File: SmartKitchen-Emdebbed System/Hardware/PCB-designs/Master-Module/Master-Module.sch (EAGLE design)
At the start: 20 parts, among them IC2 7805DT, J1 RJ11-2L-B, J2 RJ11-2L-B, J3 RJ11-2L-B, J4 RJ11-2L-B, Q1 BSS123, X1 K375M

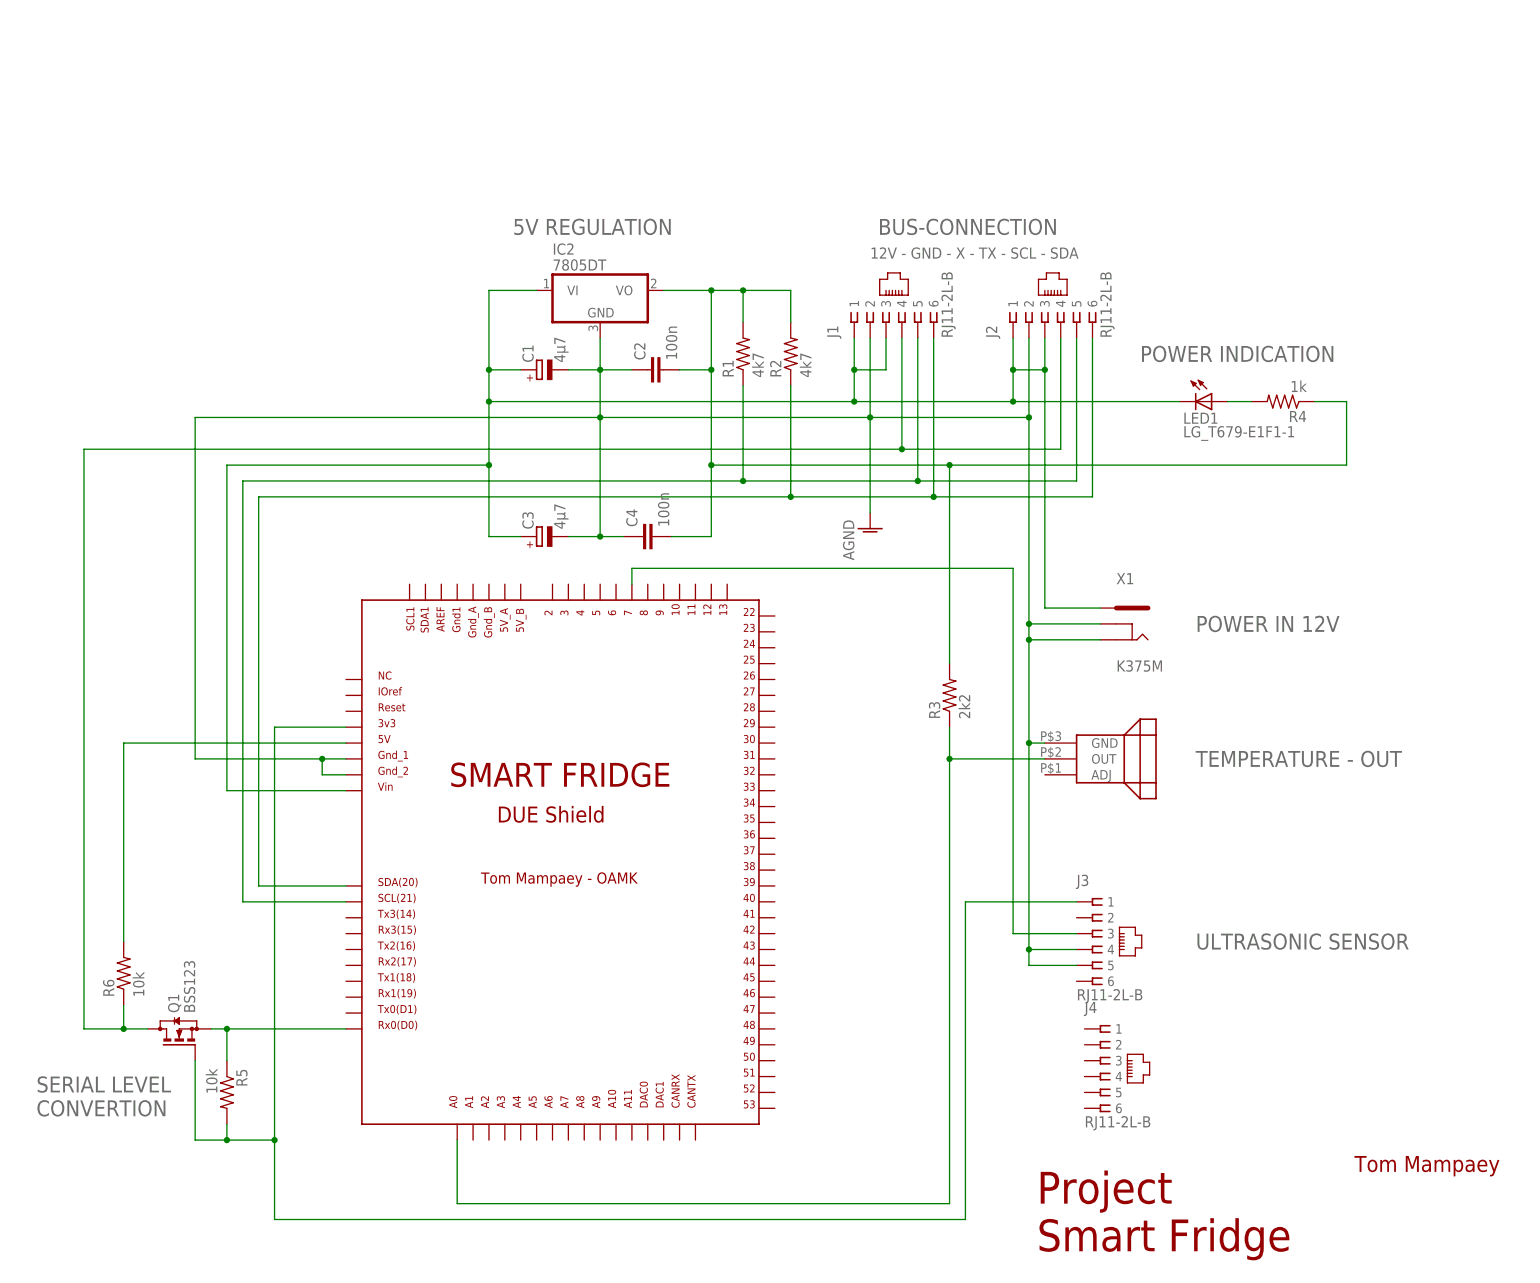
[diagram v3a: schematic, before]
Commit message: Complete redesing Master for Wifi-port
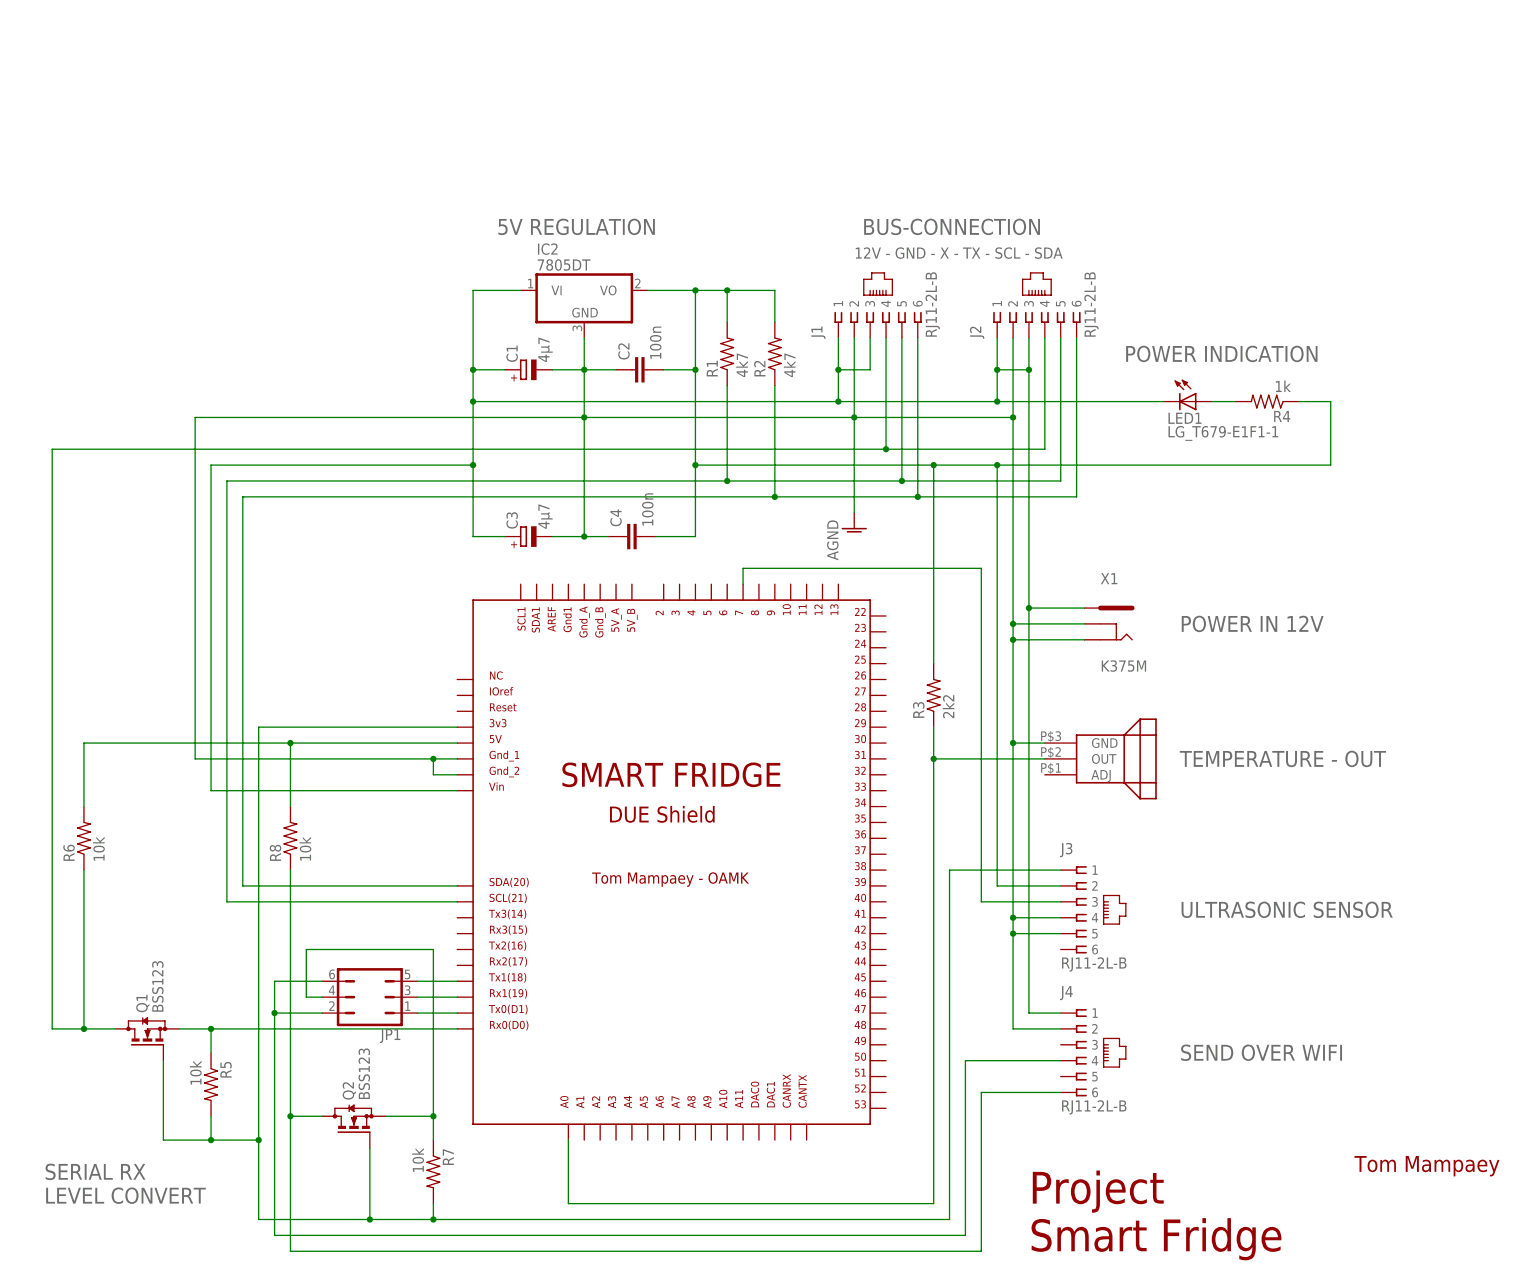
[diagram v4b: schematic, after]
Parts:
- added JP1: (no value), jumper:JP3Q
- added Q2: BSS123, transistor-small-signal:BSS123
- added R7, R8: 10k, rcl:R-US_R0402
- J4: MF (none) -> TYCO ELECTRONICS; MPN (none) -> RJ11-2L-B; OC_FARNELL (none) -> unknown; OC_NEWARK (none) -> 83F4463
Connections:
- new net N$11: JP1.1, U$1.TX0
- new net N$30: JP1.3, U$1.RX1
- new net N$31: JP1.5, U$1.TX1
- new net N$33: J4.4, JP1.2, JP1.6
- new net N$34: J4.6, Q2.D, R8.1
- new net N$35: JP1.4, Q2.S, R7.1
- net AGND: now also J4.2
- net N$10: now also J4.1
- net N$14: now also Q2.G, R7.2
- net N$4: now also R8.2
- net N$8: now also J3.2
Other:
- note added: "SEND OVER WIFI"
- note added: "SERIAL RX LEVEL CONVERT"
- note removed: "SERIAL LEVEL CONVERTION"
- moved on the sheet: C1, C2, C3, C4, IC2, J1, J2, J3, J4, LED1, Q1, R1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

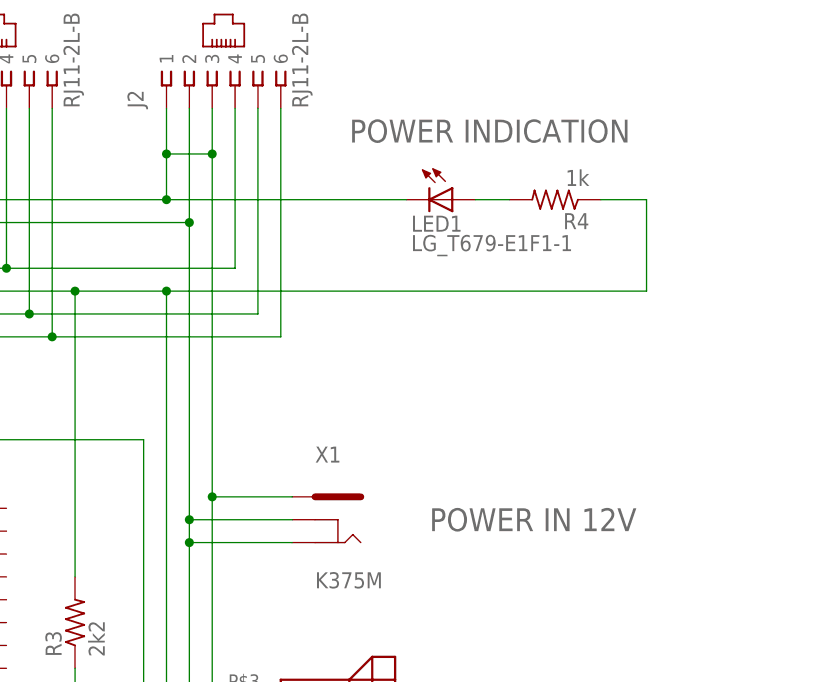
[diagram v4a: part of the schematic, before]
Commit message: Redesigned wrong component
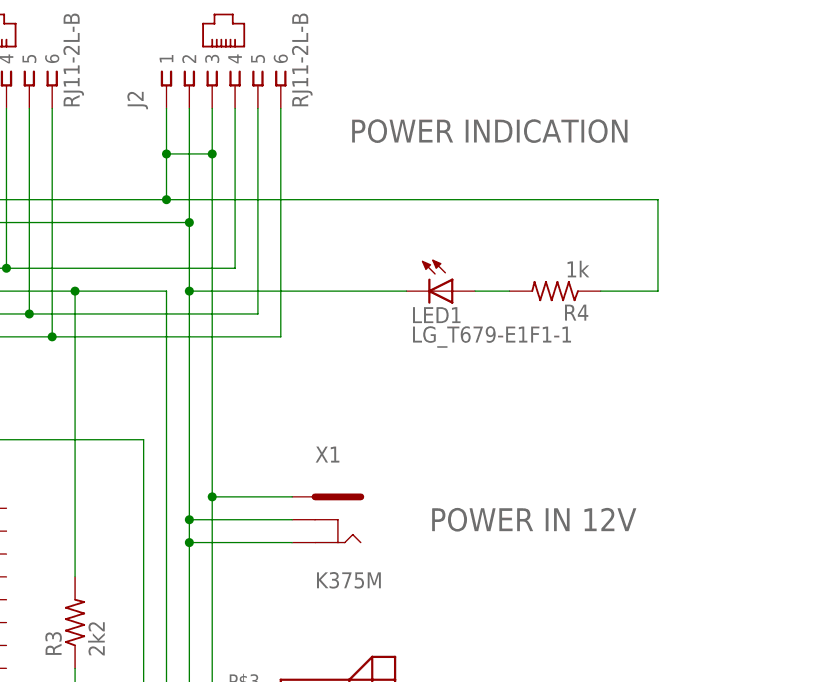
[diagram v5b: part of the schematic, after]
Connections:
- removed net N$10: C1.+, C3.+, IC2.VI, J1.1, J1.3, J2.1, J2.3, J4.1, LED1.C, U$1.VIN, X1.1
- new net N$47: C1.+, C3.+, IC2.VI, J1.1, J1.3, J2.1, J2.3, J4.1, R4.1, U$1.VIN, X1.1
- net AGND: now also LED1.C
- net N$8: no longer R4.1
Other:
- moved on the sheet: LED1, R4
